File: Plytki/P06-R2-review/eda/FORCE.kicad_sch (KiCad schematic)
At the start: 6 parts, among them J3 ISERIES, J4 SW1 A, J5 SW1 B, SW1 DPDT ON-ON

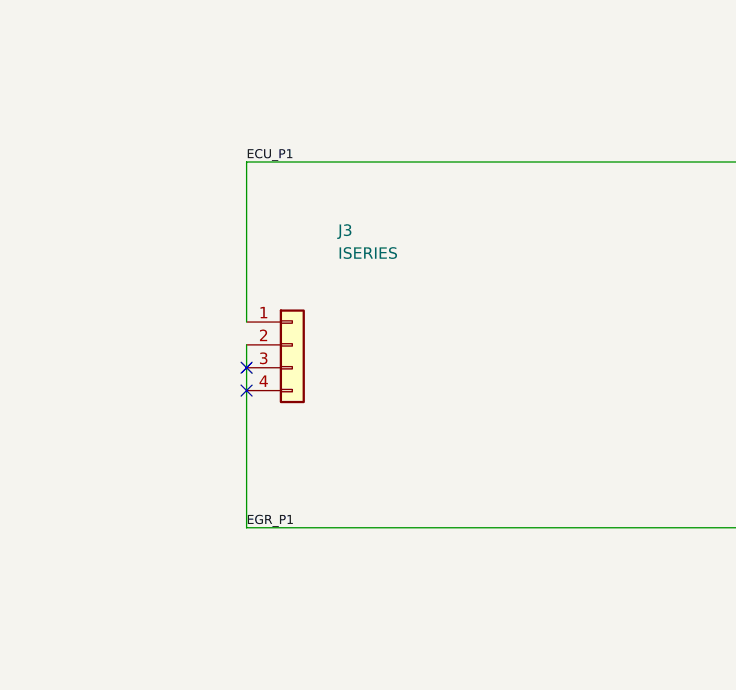
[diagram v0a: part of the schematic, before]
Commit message: P06 R2: przegląd lokalny schematu — J3 2 pola, J4 raster 7,62 mm, RSH1 WSK25125L000FEA z polami według karty
- J3/J4/J5 z wymiarami R1 potrzebują 81 mm krawędzi x = 0, między strefami M3 jest 65 mm: J3 bez pustych
  pól 3/4 (numeracja od drugiego końca), J4 raster 7,62 mm zamiast 17,78 mm.
- RSH1: kod według karty Vishay 30108 (poniżej 0,01 Ω zapis z L: WSK25125L000FEA); 1 W przy 70 °C, TCR
  ±35 ppm/K; footprint lokalny z polami pomiarowymi 1,70 mm (tabela karty; biblioteka KiCada 1,40 mm).
- R21 PR02 THT zostaje (decyzja użytkownika 1.10).
- ERC 0, 243/243 pinów, elektryczne 33/33 (mutacje 30/30), S1 27/27 (mutacje 37/37).

Co-Authored-By: Claude Opus 5.5 <noreply@anthropic.com>
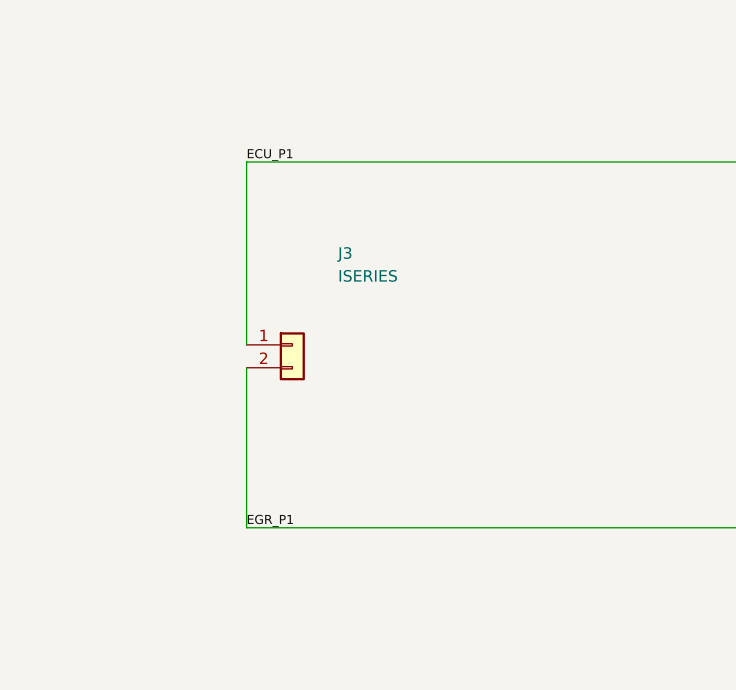
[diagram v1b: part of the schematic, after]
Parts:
- J3: symbol P06:Conn_01x04 -> P06:Conn_01x02
- RSH1: footprint Resistor_SMD:R_Shunt_Vishay_WSK2512_6332Metric_T1.19mm -> P06:R_Shunt_Vishay_WSK2512_T1.19mm_SenseE1.70; MPN WSK2512R0050FEA (Vishay WSK2512, 5 mOhm 1%, 4-terminal; alt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 -> WSK25125L000FEA (Vishay WSK2512, 5 mOhm 1%, 1 W at 70 C, TC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
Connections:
- no-connect marks 3 -> 1
